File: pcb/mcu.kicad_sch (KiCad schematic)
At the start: 43 parts, among them J2 Fermion 1.8" TFT LCD, J4 Potentiometer, J4 UART, J7 SWD, SW1 SW_Push, SW2 SW_Push, U1 STM32F411CEU6, Y1 25MHz 9pF

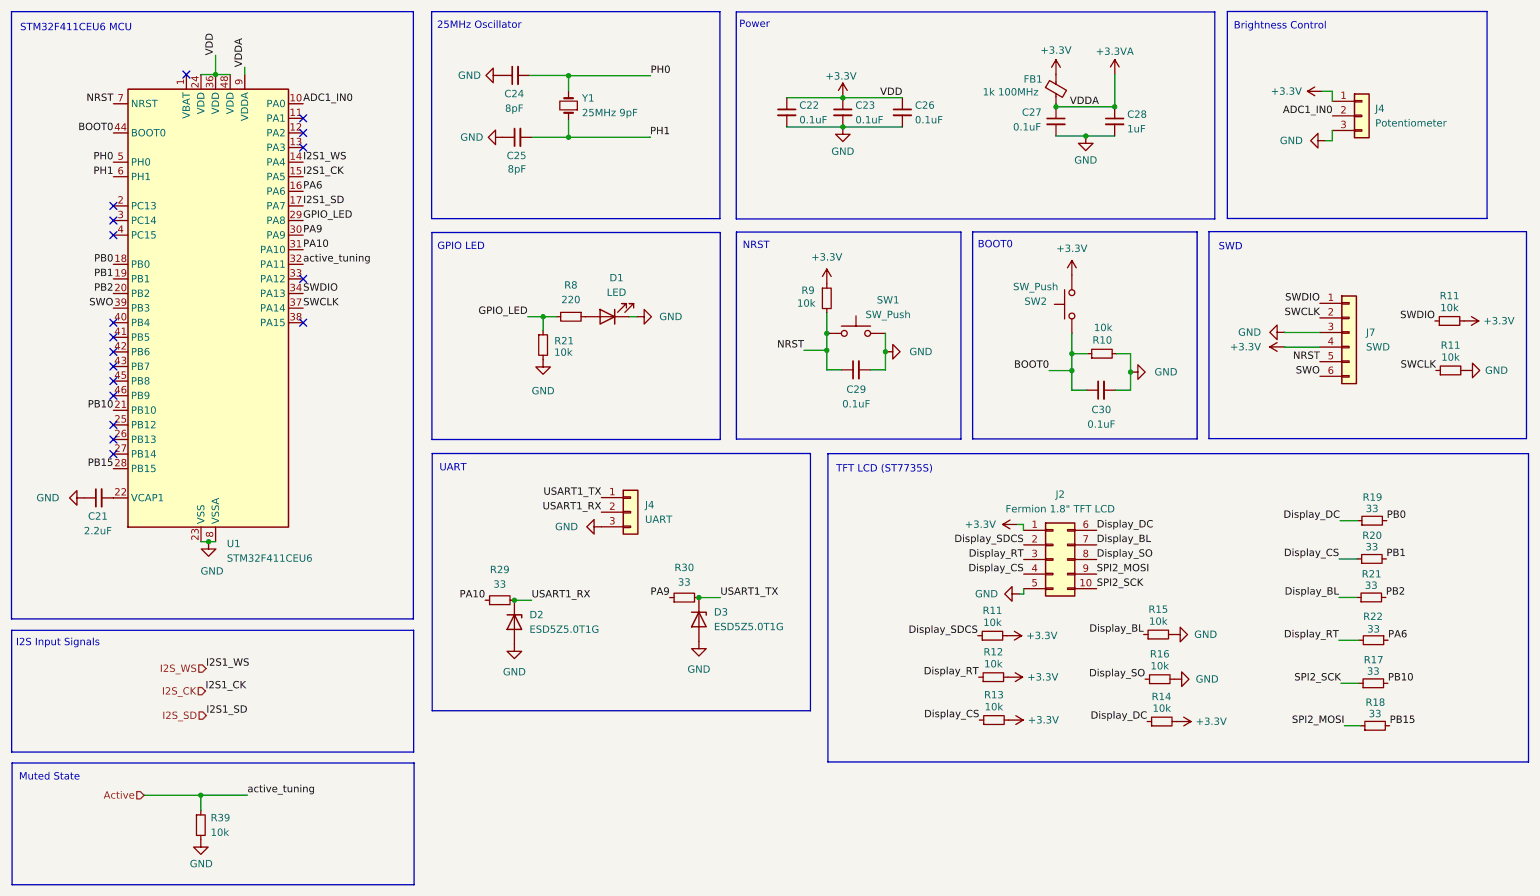
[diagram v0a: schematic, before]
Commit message: Reordered components
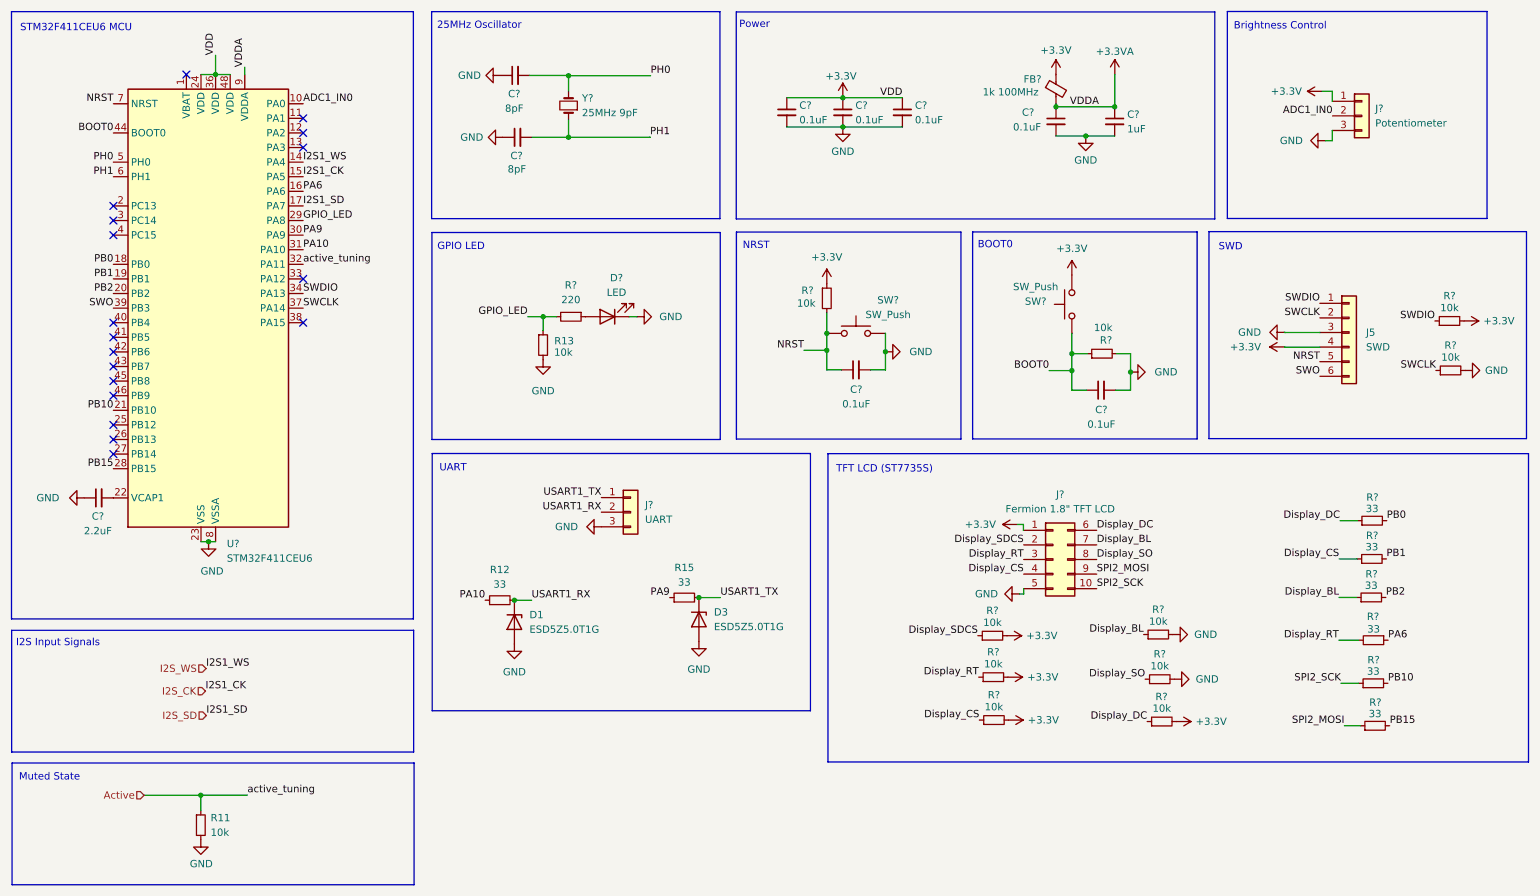
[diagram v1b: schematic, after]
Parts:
- renumbered C25 to C?, C26 to C?, C27 to C?, C28 to C?, C23 to C?, C30 to C?, C24 to C?, C29 to C?, C21 to C?, C22 to C?, D2 to D1, D1 to D?, FB1 to FB?, J7 to J5, J2 to J?, J4 to J?, R39 to R11, R29 to R12, R21 to R13, R30 to R15, R16 to R?, R19 to R?, R20 to R?, R13 to R?, R11 to R?, R18 to R?, R9 to R?, R8 to R?, R21 to R?, R12 to R?, R22 to R?, R14 to R?, R10 to R?, R15 to R?, R17 to R?, SW1 to SW?, SW2 to SW?, U1 to U?, Y1 to Y?

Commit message: Attached backlight to timer capable pin
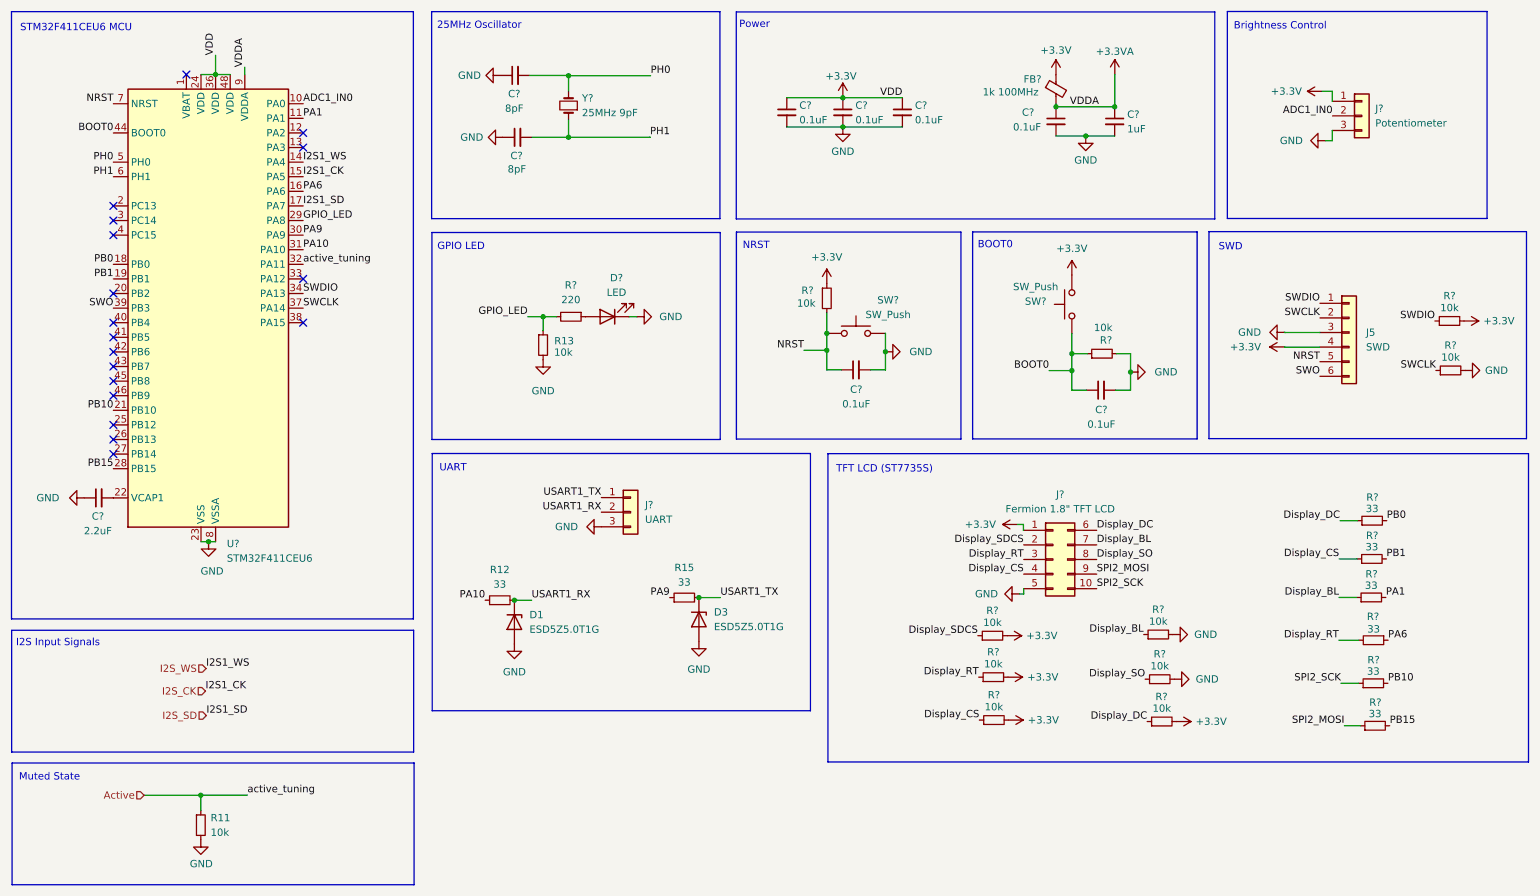
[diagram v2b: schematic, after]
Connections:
- net PA1: now reaches U?.11 (PA1)
- net PA1: now also R?.2
- net PB2: no longer names the net of U?.20 (PB2)
- net PB2: no longer R?.2
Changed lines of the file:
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@@
   (no_connect (at 47.4726 26.3144))
   (no_connect (at 67.7926 39.0144))
-  (no_connect (at 67.7926 33.9344))
   (no_connect (at 34.7726 92.3544))
   (no_connect (at 34.7726 74.5744))
@@
   (no_connect (at 34.7726 51.7144))
   (no_connect (at 34.7726 89.8144))
+  (no_connect (at 34.7726 64.4144))
   (no_connect (at 34.7726 49.1744))
   (no_connect (at 34.7726 54.2544))
@@
     (effects (font (size 1.27 1.27)) (justify left bottom))
   )
+  (label "PA1" (at 67.7926 33.9344 0) (fields_autoplaced)
+    (effects (font (size 1.27 1.27)) (justify left bottom))
+  )
   (label "BOOT0" (at 197.5866 77.8256 180) (fields_autoplaced)
     (effects (font (size 1.27 1.27)) (justify right bottom))
@@
     (effects (font (size 1.27 1.27)) (justify right bottom))
   )
-  (label "PB2" (at 34.7726 64.4144 180) (fields_autoplaced)
-    (effects (font (size 1.27 1.27)) (justify right bottom))
-  )
   (label "PA9" (at 67.7926 54.2544 0) (fields_autoplaced)
     (effects (font (size 1.27 1.27)) (justify left bottom))
@@
     (effects (font (size 1.27 1.27)) (justify right bottom))
   )
-  (label "PB2" (at 256.1844 117.2972 0) (fields_autoplaced)
-    (effects (font (size 1.27 1.27)) (justify left bottom))
-  )
+  (label "PA1" (at 256.1844 117.2972 0) (fields_autoplaced)
+    (effects (font (size 1.27 1.27)) (justify left bottom))
+  )

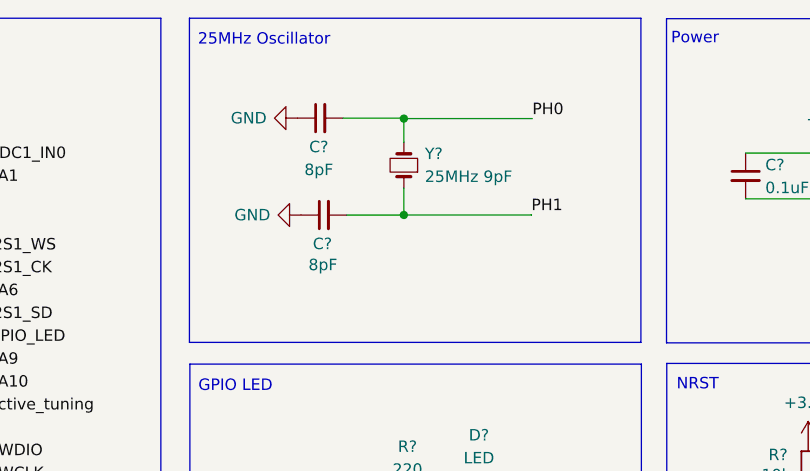
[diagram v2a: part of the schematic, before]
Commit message: Assigned footprints and jlcpcb part number to all components
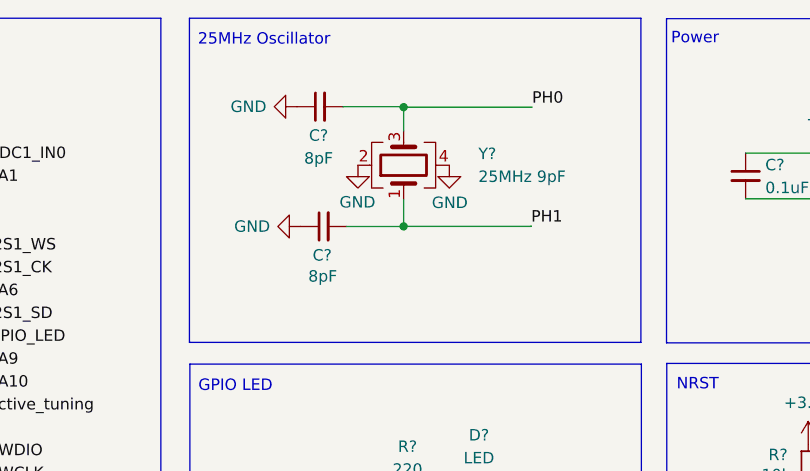
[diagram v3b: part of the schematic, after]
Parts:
- C? (x2): footprint (none) -> Capacitor_SMD:C_0603_1608Metric; LCSC (none) -> C346204; MPN (none) -> CL10C080DB81PNC; Manufacturer (none) -> Samsung Electro-Mechanics
- C? (x6): footprint (none) -> Capacitor_SMD:C_1206_3216Metric; LCSC (none) -> C577121; MPN (none) -> CC1206JKNPO9BN104; Manufacturer (none) -> Yageo
- C?: footprint (none) -> Capacitor_SMD:C_0805_2012Metric; LCSC (none) -> C1712; MPN (none) -> CL21B105KAFNFNE; Manufacturer (none) -> Samsung Electro-Mechanics
- C?: footprint (none) -> Capacitor_SMD:C_0805_2012Metric; LCSC (none) -> C19110; MPN (none) -> CL21B225KAFNNNE; Manufacturer (none) -> Samsung Electro-Mechanics
- D1, D3: LCSC (none) -> C82044; MPN (none) -> ESD5Z5.0T1G; Manufacturer (none) -> onsemi
- D?: footprint (none) -> LED_SMD:LED_0603_1608Metric; LCSC (none) -> C2286; MPN (none) -> KT-0603R; Manufacturer (none) -> Hubei KENTO Elec
- FB?: footprint (none) -> Inductor_SMD:L_1806_4516Metric; LCSC (none) -> C88999; MPN (none) -> BLM41PG102SN1L; Manufacturer (none) -> Murata
- R11, R13, R? (x10): footprint (none) -> Resistor_SMD:R_0603_1608Metric; LCSC (none) -> C98220; MPN (none) -> RC0603FR-0710KL; Manufacturer (none) -> Yageo
- R12, R15, R? (x6): footprint (none) -> Resistor_SMD:R_0603_1608Metric; LCSC (none) -> C108661; MPN (none) -> RC0603FR-0733RL; Manufacturer (none) -> Yageo
- R?: footprint (none) -> Resistor_SMD:R_0603_1608Metric; LCSC (none) -> C107696; MPN (none) -> RC0603FR-07220RL; Manufacturer (none) -> Yageo
- SW? (x2): footprint Button_Switch_SMD:SW_SPST_Omron_B3FS-100xP -> Button_Switch_SMD:SW_Push_1P1T_NO_6x6mm_H9.5mm; LCSC (none) -> C273519; MPN (none) -> TL3301AF160QG; Manufacturer (none) -> E-Switch
- U?: LCSC (none) -> C60420; MPN (none) -> STM32F411CEU6; Manufacturer (none) -> STMicroelectronics
- Y?: footprint (none) -> Crystal:Crystal_SMD_3225-4Pin_3.2x2.5mm; symbol Device:Crystal_Small -> Device:Crystal_GND24; LCSC (none) -> C2981679; MPN (none) -> 3225-25-9-10-10/A; Manufacturer (none) -> Suzhou Liming Elec
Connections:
- net GND: now also Y?.2, Y?.4
- net PH0: now also Y?.3; no longer Y?.2
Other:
- moved on the sheet: C?

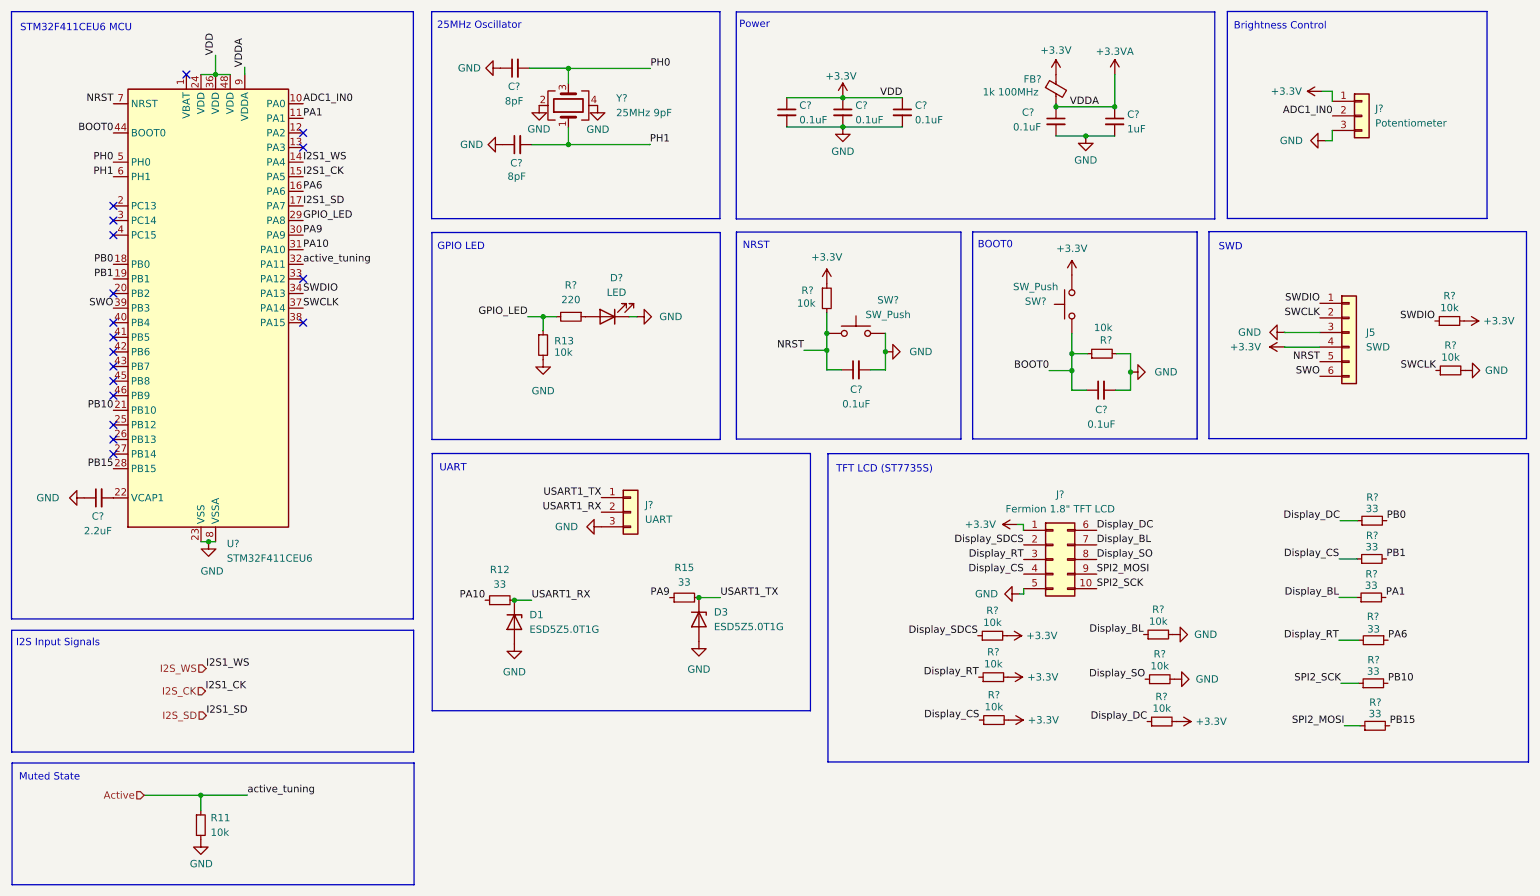
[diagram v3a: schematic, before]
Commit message: ERC fixes
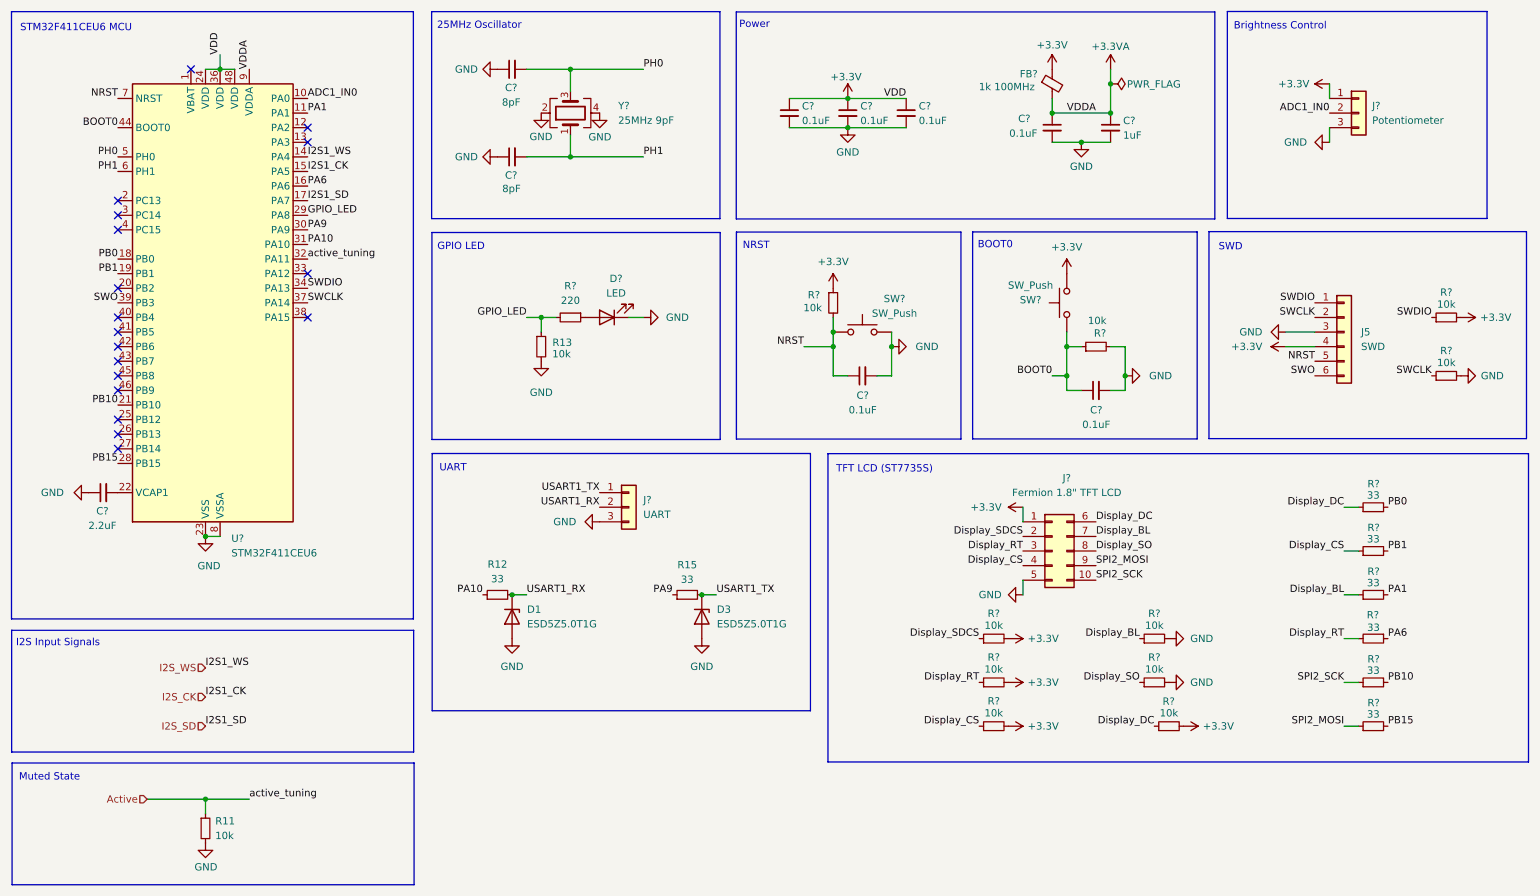
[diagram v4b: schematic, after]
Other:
- moved on the sheet: C?, D1, D3, FB?, J5, J?, R11, R12, R15, R?, SW?, U?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

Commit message: Starting PCB layout
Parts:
- SW?: value SW_Push -> NRST
- SW?: value SW_Push -> BOOT0
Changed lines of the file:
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@@
       (effects (font (size 1.27 1.27)))
     )
-    (property "Value" "SW_Push" (at 170.688 67.8688 0)
+    (property "Value" "NRST" (at 170.688 67.8688 0)
       (effects (font (size 1.27 1.27)))
     )
@@
   (symbol (lib_id "Switch:SW_Push") (at 200.66 66.04 90) (unit 1)
     (in_bom yes) (on_board yes) (dnp no)
-    (property "Reference" "SW?" (at 194.3608 65.532 90)
-      (effects (font (size 1.27 1.27)))
-    )
-    (property "Value" "SW_Push" (at 194.3608 62.992 90)
+    (property "Reference" "SW?" (at 194.2084 61.7728 90)
+      (effects (font (size 1.27 1.27)))
+    )
+    (property "Value" "BOOT0" (at 194.4116 64.516 90)
       (effects (font (size 1.27 1.27)))
     )
@@
   (symbol (lib_id "Device:R_Small") (at 160.02 66.04 0) (unit 1)
     (in_bom yes) (on_board yes) (dnp no)
-    (property "Reference" "R?" (at 155.6004 64.6684 0)
-      (effects (font (size 1.27 1.27)) (justify left))
-    )
+    (property "Reference" "R?" (at 154.686 64.6176 0)
+      (effects (font (size 1.27 1.27)) (justify left))
+    )

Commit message: First revision of the pcb layout
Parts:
- removed R? (x2): 10k, Resistor_SMD:R_0603_1608Metric, symbol Device:R_Small
- C? (x2): footprint Capacitor_SMD:C_0603_1608Metric -> Capacitor_SMD:C_0402_1005Metric; LCSC C346204 -> C1578; MPN CL10C080DB81PNC -> 0402CG8R0C500NT; Manufacturer Samsung Electro-Mechanics -> FH (Guangdong Fenghua Advanced Tech)
- C? (x6): footprint Capacitor_SMD:C_1206_3216Metric -> Capacitor_SMD:C_0402_1005Metric; LCSC C577121 -> C1525; MPN CC1206JKNPO9BN104 -> CL05B104KO5NNNC; Manufacturer Yageo -> Samsung Electro-Mechanics
